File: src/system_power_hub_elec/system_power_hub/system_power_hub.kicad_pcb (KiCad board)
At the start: 6 copper layers, 66.5 x 64.6 mm, 176 parts, among them J1 XT60M, J10 XT30F, J101 SM02B-PASS, J2 XT30F, J3 XT30F, J4 XT30F, J5 XT30F, J6 IDC6, J7 XT30F, J8 XT30F, J9 XT30F, Q1 SSM3K333R, Q10 IRFH7440TRPBF, Q11 IRFH7440TRPBF, Q12 IRFH7440TRPBF, Q13 Q_Dual_NPN_NPN_E1B1C2E2B2C1, Q15 IRFH7440TRPBF, Q16 IRFH7440TRPBF, Q2 Q_Dual_NPN_NPN_E1B1C2E2B2C1, Q4 IRFH7440TRPBF, Q6 Q_Dual_NPN_NPN_E1B1C2E2B2C1, Q7 IRFH7440TRPBF, Q8 Q_Dual_NPN_NPN_E1B1C2E2B2C1, Q9 IRFH7440TRPBF, U1 STM32G474RBT6, U102 TCAN1462V, U220 MP2459GJ-Z-MS, U230 AP62200TWU, U240 HX4002, U4 24LC128, Y1 24MHz

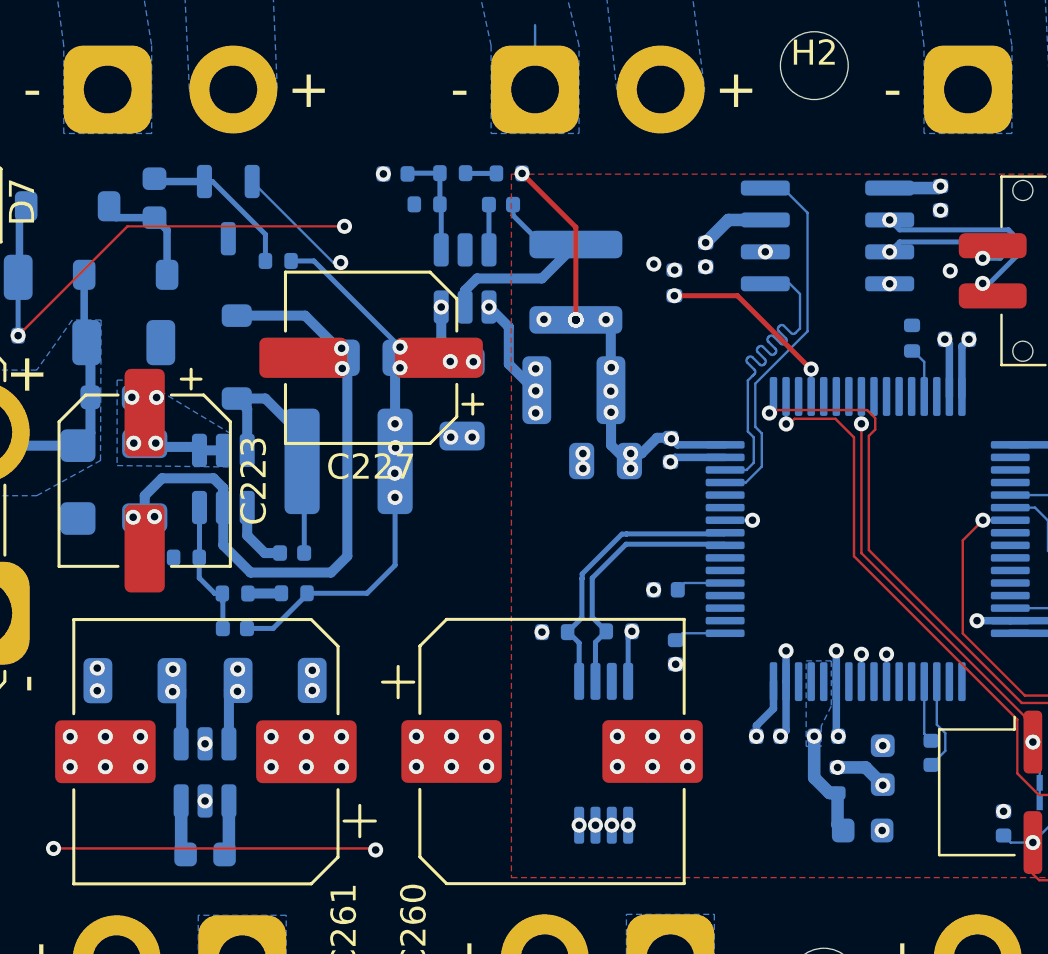
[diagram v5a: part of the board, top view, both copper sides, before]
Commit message: Mosfet DGS -> GSD, CAN tranceiver STB -> GND
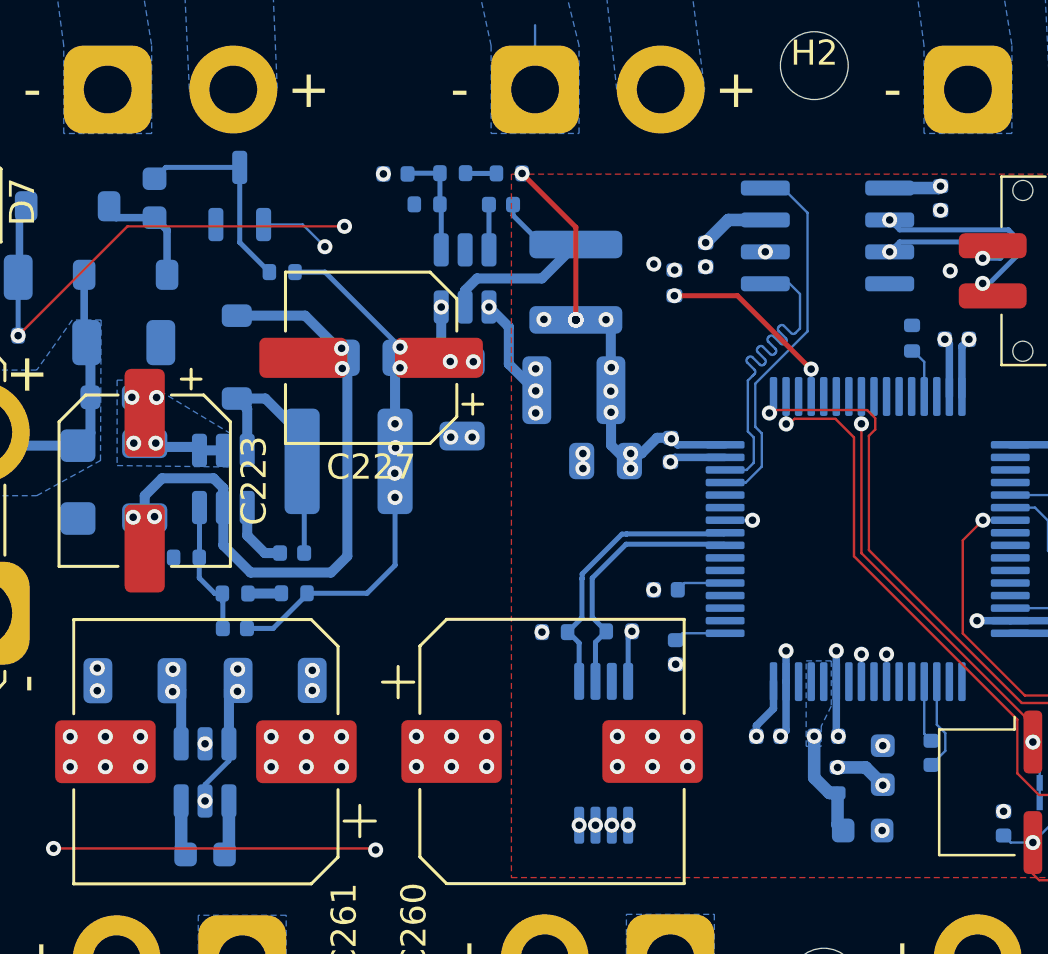
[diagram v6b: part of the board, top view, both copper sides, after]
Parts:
- moved Q1 0.72 mm to (86.9, 74.9), turned to 90 degrees
- moved R8 0.47 mm to (88.6, 77.9)
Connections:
- Q1 pad 1: Net-(Q1-D) -> /Analog Stuff/clk_in
- Q1 pad 2: /Analog Stuff/clk_in -> GND
- Q1 pad 3: GND -> Net-(Q1-D)
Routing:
- net VDD: track 65.4 -> 68.0 mm
- net Net-(Q1-D): track 6.39 -> 8.23 mm
- net /Analog Stuff/clk_in: track 17.6 -> 16.4 mm
- net GND: vias 124 -> 123
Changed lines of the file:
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@@
 			(size 2.7 2.7)
 			(drill 2.7)
-			(layers "F&B.Cu" "*.Mask")
+			(layers "*.Cu" "*.Mask")
 		)
 		(embedded_fonts no)
@@
 			(size 2.7 2.7)
 			(drill 2.7)
-			(layers "F&B.Cu" "*.Mask")
+			(layers "*.Cu" "*.Mask")
 		)
 		(embedded_fonts no)
@@
 			(size 2.7 2.7)
 			(drill 2.7)
-			(layers "F&B.Cu" "*.Mask")
+			(layers "*.Cu" "*.Mask")
 		)
 		(embedded_fonts no)
@@
 			(size 2.7 2.7)
 			(drill 2.7)
-			(layers "F&B.Cu" "*.Mask")
+			(layers "*.Cu" "*.Mask")
 		)
 		(embedded_fonts no)
@@
 	(footprint "Resistor_SMD:R_0402_1005Metric"
 		(layer "B.Cu")
-		(at 88.413427 77.457948 180)
+		(at 88.57 77.9 180)
 		(descr "Resistor SMD 0402 (1005 Metric), square (rectangular) end terminal, IPC-7351 nominal, (Body size source: IPC-SM-782 page 72, https://www.pcb-3d.com/wordpress/wp-content/uploads/ipc-sm-782a_amendment_1_and_2.pdf), generated with kicad-footprint-generator")
 		(tags "resistor")
@@
 	(footprint "Package_TO_SOT_SMD:SOT-23-3"
 		(layer "B.Cu")
-		(at 86.425927 75.432948 -90)
+		(at 86.88 74.87 90)
 		(descr "SOT, 3 Pin (JEDEC MO-178 inferred 3-pin variant https://www.jedec.org/document_search?search_api_views_fulltext=MO-178), generated with kicad-footprint-generator ipc_gullwing_generator.py")
 		(tags "SOT TO_SOT_SMD")
@@
 			)
 		)
-		(property "Description" "N-MOSFET transistor, drain/gate/source"
+		(property "Description" "N-MOSFET transistor, gate/source/drain"
 			(at 0 0 90)
 			(layer "B.Fab")
@@
 		(attr smd)
 		(fp_line
-			(start 0 1.560001)
-			(end -0.8 1.56)
+			(start 0 -1.560001)
+			(end 0.8 -1.56)
 			(stroke
 				(width 0.12)
@@
 		)
 		(fp_line
-			(start 0 1.560001)
-			(end 0.8 1.56)
+			(start 0 -1.560001)
+			(end -0.8 -1.56)
 			(stroke
 				(width 0.12)
@@
 		)
 		(fp_line
-			(start 0 -1.560001)
-			(end -0.8 -1.56)
+			(start 0 1.560001)
+			(end 0.8 1.56)
 			(stroke
 				(width 0.12)
@@
 		)
 		(fp_line
-			(start 0 -1.560001)
-			(end 0.8 -1.56)
+			(start 0 1.560001)
+			(end -0.8 1.56)
 			(stroke
 				(width 0.12)
@@
 		)
 		(fp_line
-			(start -1.050001 1.7)
-			(end 1.050001 1.7)
+			(start 1.050001 -1.7)
+			(end -1.050001 -1.7)
 			(stroke
 				(width 0.05)
@@
 		)
 		(fp_line
-			(start 1.050001 1.7)
-			(end 1.05 0.55)
+			(start -1.050001 -1.7)
+			(end -1.05 -1.5)
 			(stroke
 				(width 0.05)
@@
 		)
 		(fp_line
-			(start -2.05 1.5)
-			(end -1.05 1.5)
+			(start -1.05 -1.5)
+			(end -2.05 -1.5)
 			(stroke
 				(width 0.05)
@@
 		)
 		(fp_line
-			(start -1.05 1.5)
-			(end -1.050001 1.7)
+			(start -2.05 -1.5)
+			(end -2.05 1.5)
 			(stroke
 				(width 0.05)
@@
 		)
 		(fp_line
-			(start 1.05 0.55)
-			(end 2.05 0.55)
+			(start 2.05 -0.55)
+			(end 1.05 -0.55)
 			(stroke
 				(width 0.05)
@@
 		)
 		(fp_line
-			(start 2.05 0.55)
-			(end 2.05 -0.55)
+			(start 1.05 -0.55)
+			(end 1.050001 -1.7)
 			(stroke
 				(width 0.05)
@@
 		)
 		(fp_line
-			(start 1.05 -0.55)
-			(end 1.050001 -1.7)
+			(start 2.05 0.55)
+			(end 2.05 -0.55)
 			(stroke
 				(width 0.05)
@@
 		)
 		(fp_line
-			(start 2.05 -0.55)
-			(end 1.05 -0.55)
+			(start 1.05 0.55)
+			(end 2.05 0.55)
 			(stroke
 				(width 0.05)
@@
 		)
 		(fp_line
-			(start -2.05 -1.5)
-			(end -2.05 1.5)
+			(start -1.05 1.5)
+			(end -1.050001 1.7)
 			(stroke
 				(width 0.05)
@@
 		)
 		(fp_line
-			(start -1.05 -1.5)
-			(end -2.05 -1.5)
+			(start -2.05 1.5)
+			(end -1.05 1.5)
 			(stroke
 				(width 0.05)
@@
 		)
 		(fp_line
-			(start -1.050001 -1.7)
-			(end -1.05 -1.5)
+			(start 1.050001 1.7)
+			(end 1.05 0.55)
 			(stroke
 				(width 0.05)
@@
 		)
 		(fp_line
-			(start 1.050001 -1.7)
-			(end -1.050001 -1.7)
+			(start -1.050001 1.7)
+			(end 1.050001 1.7)
 			(stroke
 				(width 0.05)
@@
 		)
 		(fp_line
-			(start -0.4 1.45)
-			(end 0.8 1.45)
+			(start 0.8 -1.45)
+			(end -0.8 -1.45)
 			(stroke
 				(width 0.1)
@@
 		)
 		(fp_line
-			(start 0.8 1.45)
-			(end 0.8 -1.45)
+			(start -0.8 -1.45)
+			(end -0.8 1.050001)
 			(stroke
 				(width 0.1)
@@
 		)
 		(fp_line
-			(start -0.8 -1.45)
-			(end -0.8 1.050001)
+			(start 0.8 1.45)
+			(end 0.8 -1.45)
 			(stroke
 				(width 0.1)
@@
 		)
 		(fp_line
-			(start 0.8 -1.45)
-			(end -0.8 -1.45)
+			(start -0.4 1.45)
+			(end 0.8 1.45)
 			(stroke
 				(width 0.1)
@@
 		)
 		(pad "1" smd roundrect
-			(at -1.1375 0.949999 270)
+			(at -1.1375 0.949999 90)
 			(size 1.325 0.6)
 			(layers "B.Cu" "B.Mask" "B.Paste")
 			(roundrect_rratio 0.25)
-			(net 14 "Net-(Q1-D)")
-			(pinfunction "D")
-			(pintype "passive")
+			(net 40 "/Analog Stuff/clk_in")
+			(pinfunction "G")
+			(pintype "input")
 		)
 		(pad "2" smd roundrect
-			(at -1.1375 -0.949999 270)
+			(at -1.1375 -0.949999 90)
 			(size 1.325 0.6)
 			(layers "B.Cu" "B.Mask" "B.Paste")
 			(roundrect_rratio 0.25)
-			(net 40 "/Analog Stuff/clk_in")
-			(pinfunction "G")
-			(pintype "input")
+			(net 1 "GND")
+			(pinfunction "S")
+			(pintype "passive")
 		)
 		(pad "3" smd roundrect
-			(at 1.1375 0 270)
+			(at 1.1375 0 90)
 			(size 1.325 0.6)
 			(layers "B.Cu" "B.Mask" "B.Paste")
 			(roundrect_rratio 0.25)
-			(net 1 "GND")
-			(pinfunction "S")
+			(net 14 "Net-(Q1-D)")
+			(pinfunction "D")
 			(pintype "passive")
 		)
@@
 	)
 	(via
-		(at 112.75 78.365)
-		(size 0.6)
-		(drill 0.3)
-		(layers "F.Cu" "B.Cu")
-		(net 1)
-	)
-	(via
 		(at 76.6 101.555)
 		(size 0.6)
@@
 	)
 	(segment
+		(start 86.449999 97.350001)
+		(end 86.449999 96.675)
+		(width 0.2)
+		(layer "B.Cu")
+		(net 4)
+	)
+	(segment
 		(start 119.544999 92.275)
 		(end 119.825 92.555001)
@@
 	)
 	(segment
+		(start 85.5 98.3)
+		(end 86.449999 97.350001)
+		(width 0.2)
+		(layer "B.Cu")
+		(net 4)
+	)
+	(segment
+		(start 85.5 98.95)
+		(end 85.5 98.3)
+		(width 0.2)
+		(layer "B.Cu")
+		(net 4)
+	)
+	(segment
 		(start 86.449999 94.5175)
 		(end 86.814999 94.1525)
@@
 	)
 	(segment
-		(start 87.903428 76.397949)
-		(end 87.903428 77.457948)
+		(start 86.88 73.7325)
+		(end 86.88 76.719999)
 		(width 0.2)
 		(layer "B.Cu")
@@
 	)
 	(segment
-		(start 85.800927 74.295448)
-		(end 87.903428 76.397949)
+		(start 83.488427 74.182948)
+		(end 83.938875 73.7325)
 		(width 0.2)
 		(layer "B.Cu")
@@
 	)
 	(segment
-		(start 85.475928 74.295448)
-		(end 85.800927 74.295448)
+		(start 83.938875 73.7325)
+		(end 86.88 73.7325)
 		(width 0.2)
 		(layer "B.Cu")
@@
 	)
 	(segment
-		(start 83.600927 74.295448)
-		(end 83.488427 74.182948)
-		(width 0.3)
-		(layer "B.Cu")
-		(net 14)
-	)
-	(segment
-		(start 85.475928 74.295448)
-		(end 83.600927 74.295448)
-		(width 0.3)
+		(start 86.88 76.719999)
+		(end 88.060001 77.9)
+		(width 0.2)
 		(layer "B.Cu")
 		(net 14)
@@
 	)
 	(segment
-		(start 89.832947 77.457948)
-		(end 93.259999 80.885)
+		(start 91.948427 90.682948)
+		(end 89.558427 90.682948)
 		(width 0.2)
 		(layer "B.Cu")
@@
 	)
 	(segment
-		(start 91.948427 90.682948)
-		(end 89.558427 90.682948)
+		(start 90.274999 77.9)
+		(end 93.259999 80.885)
 		(width 0.2)
 		(layer "B.Cu")
@@
 	)
 	(segment
-		(start 88.923426 77.457948)
-		(end 89.832947 77.457948)
+		(start 89.079999 77.9)
+		(end 90.274999 77.9)
 		(width 0.2)
 		(layer "B.Cu")
@@
 	)
 	(via
-		(at 90.9 77.52)
+		(at 90.27 76.89)
 		(size 0.6)
 		(drill 0.3)
@@
 	)
 	(segment
-		(start 87.375926 74.295448)
-		(end 90.600478 77.52)
+		(start 89.3875 76.0075)
+		(end 87.829999 76.0075)
 		(width 0.095)
 		(layer "B.Cu")
@@
 	)
 	(segment
-		(start 90.600478 77.52)
-		(end 90.9 77.52)
+		(start 90.27 76.89)
+		(end 89.3875 76.0075)
 		(width 0.095)
 		(layer "B.Cu")
@@
 	)
 	(segment
-		(start 91.2115 77.8315)
-		(end 103.110376 77.8315)
+		(start 103.110376 77.8315)
+		(end 103.361876 77.58)
 		(width 0.095)
 		(layer "In3.Cu")
@@
 	)
 	(segment
-		(start 103.110376 77.8315)
-		(end 103.361876 77.58)
+		(start 91.2115 77.8315)
+		(end 103.110376 77.8315)
 		(width 0.095)
 		(layer "In3.Cu")
@@
 	)
 	(segment
-		(start 90.9 77.52)
+		(start 90.27 76.89)
 		(end 91.2115 77.8315)
 		(width 0.095)
